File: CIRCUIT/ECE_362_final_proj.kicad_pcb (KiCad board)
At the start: 2 copper layers, 21.1 x 76.3 mm, 22 parts, among them J1 Conn_01x01_Pin, J2 Conn_01x01_Pin, J3 Conn_01x28_Socket, J4 Conn_01x28_Socket, SW2 BUTTON_MODE, SW4 BUTTON_CAPTURE, U1 TL084

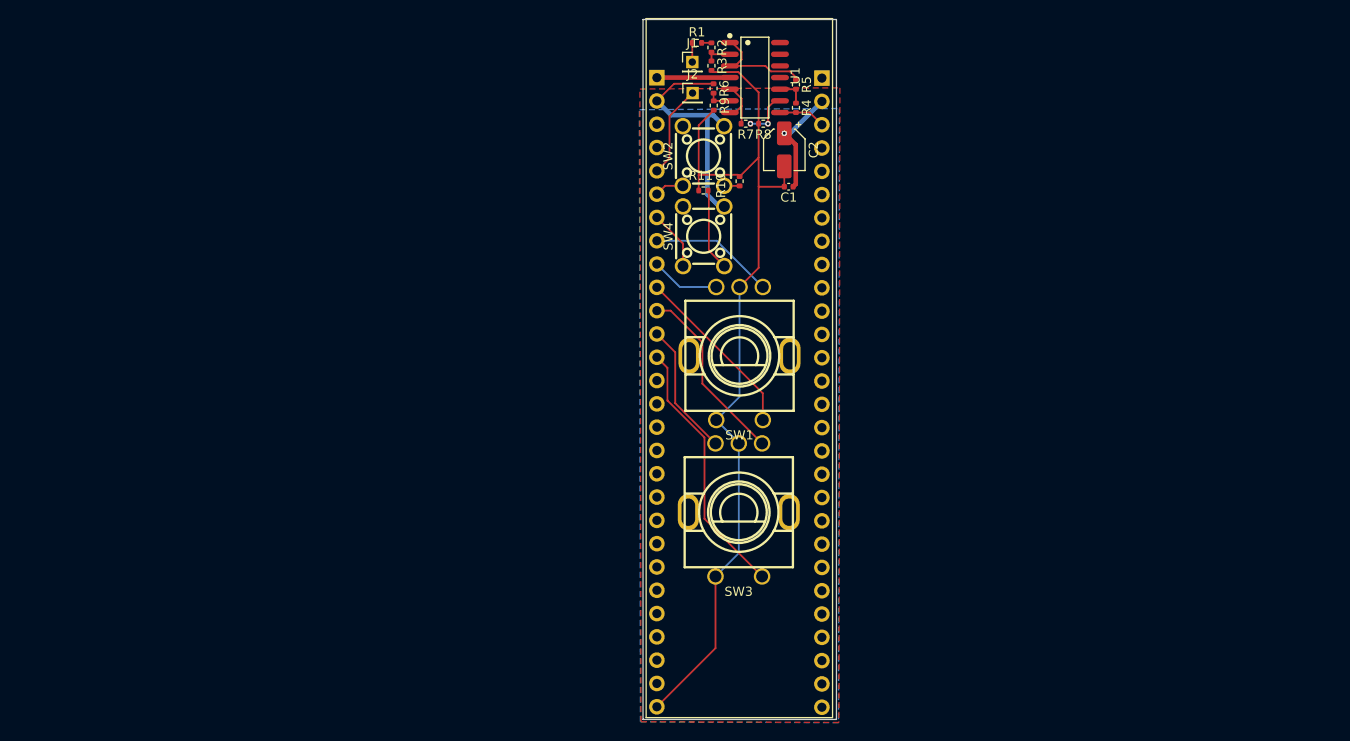
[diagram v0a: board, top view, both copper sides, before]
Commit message: added mounting holes
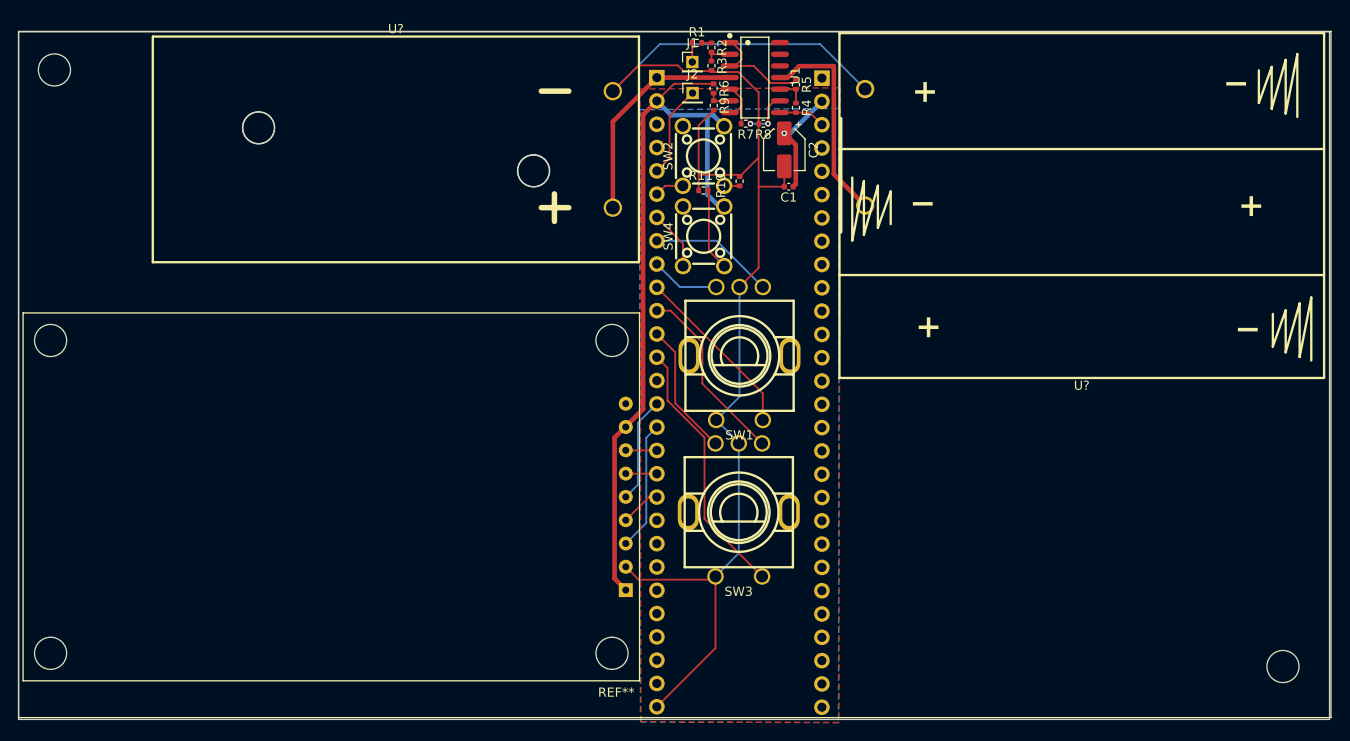
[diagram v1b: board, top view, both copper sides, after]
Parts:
- added ?: , , F.Cu at (-64.5, 5.60)
- added ?: , , F.Cu at (-42.2, 11.9)
- added ?: , , F.Cu at (69.4, 70.6)
- added ?: , , F.Cu at (-12.3, 16.6)
- added REF**: LCD_MSP2202_without_sd, LCD_MSP2202_without_sd:LCD_MSP2202_without_sd, F.Cu at (-0.72, 72.2)
- added U?: BAT-TH_2479, cell_holder_3AA:BAT-TH_2479, F.Cu at (23.9, 14.0)
- added U?: BAT-TH_2P-L53.0-W24.6-P12.70_2468, cell_holder_3AA:BAT-TH_2P-L53.0-W24.6-P12.70_2468, F.Cu at (-3.63, 14.3)
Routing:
- net +3.3V: track 38.4 -> 94.1 mm
- net GND: track 102.1 -> 156.2 mm
- net -BATT: track 0.00 -> 23.0 mm
- net +BATT: track 7.95 -> 24.1 mm
- net /GPIO13: track 0.00 -> 14.1 mm
- net /GPIO12: track 0.00 -> 11.5 mm
- net /GPIO16: track 0.00 -> 4.43 mm
- net /GPIO15: track 0.00 -> 3.40 mm
- net /GPIO14: track 0.00 -> 3.40 mm
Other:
- board size 21.1 x 76.3 mm -> 142.9 x 75 mm

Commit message: rearranged board
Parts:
- removed the ? at (-42.2, 11.9)
- removed the ? at (69.4, 70.6)
- removed the ? at (-12.3, 16.6)
- added BT2: BAT-TH_2P-L53.0-W24.6-P12.70_2468, cell_holder_3AA:BAT-TH_2P-L53.0-W24.6-P12.70_2468, B.Cu at (-6.00, 14.3)
- U?: moved to B.Cu
- moved U? 46.9 mm to (-10.6, 45.9), turned to 0 degrees
- gave numbers to parts that had none: 1
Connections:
- BT1 pad 1: GND -> BT1_GND
- REF** pad 9: x -> (no net)
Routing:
- net -BATT: track 23.0 -> 77.1 mm
- net GND: track 156.2 -> 161.8 mm
- net BT1_GND: track 0.00 -> 1.97 mm
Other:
- board size 142.9 x 75 mm -> 90.1 x 75.2 mm
